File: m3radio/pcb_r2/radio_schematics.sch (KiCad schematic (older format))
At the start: 18 parts, among them IC201 Si4460, P201 COAX

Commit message: update m3radio to si4461 (higher power variant)
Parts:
- IC201: value Si4460 -> Si4461; Farnell 2462635 -> 2462636
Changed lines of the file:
@@
 P 2550 2900
 F 0 "IC201" H 2250 3600 50  0000 L CNN
-F 1 "Si4460" H 2250 2200 50  0000 L CNN
+F 1 "Si4461" H 2250 2200 50  0000 L CNN
 F 2 "agg:QFN-20-EP-SI" H 2250 2100 50  0001 L CNN
 F 3 "" H 2150 3500 50  0001 C CNN
-F 4 "2462635" H 2250 2000 50  0001 L CNN "Farnell"
+F 4 "2462636" H 2250 2000 50  0001 L CNN "Farnell"
 	1    2550 2900
 	1    0    0    -1

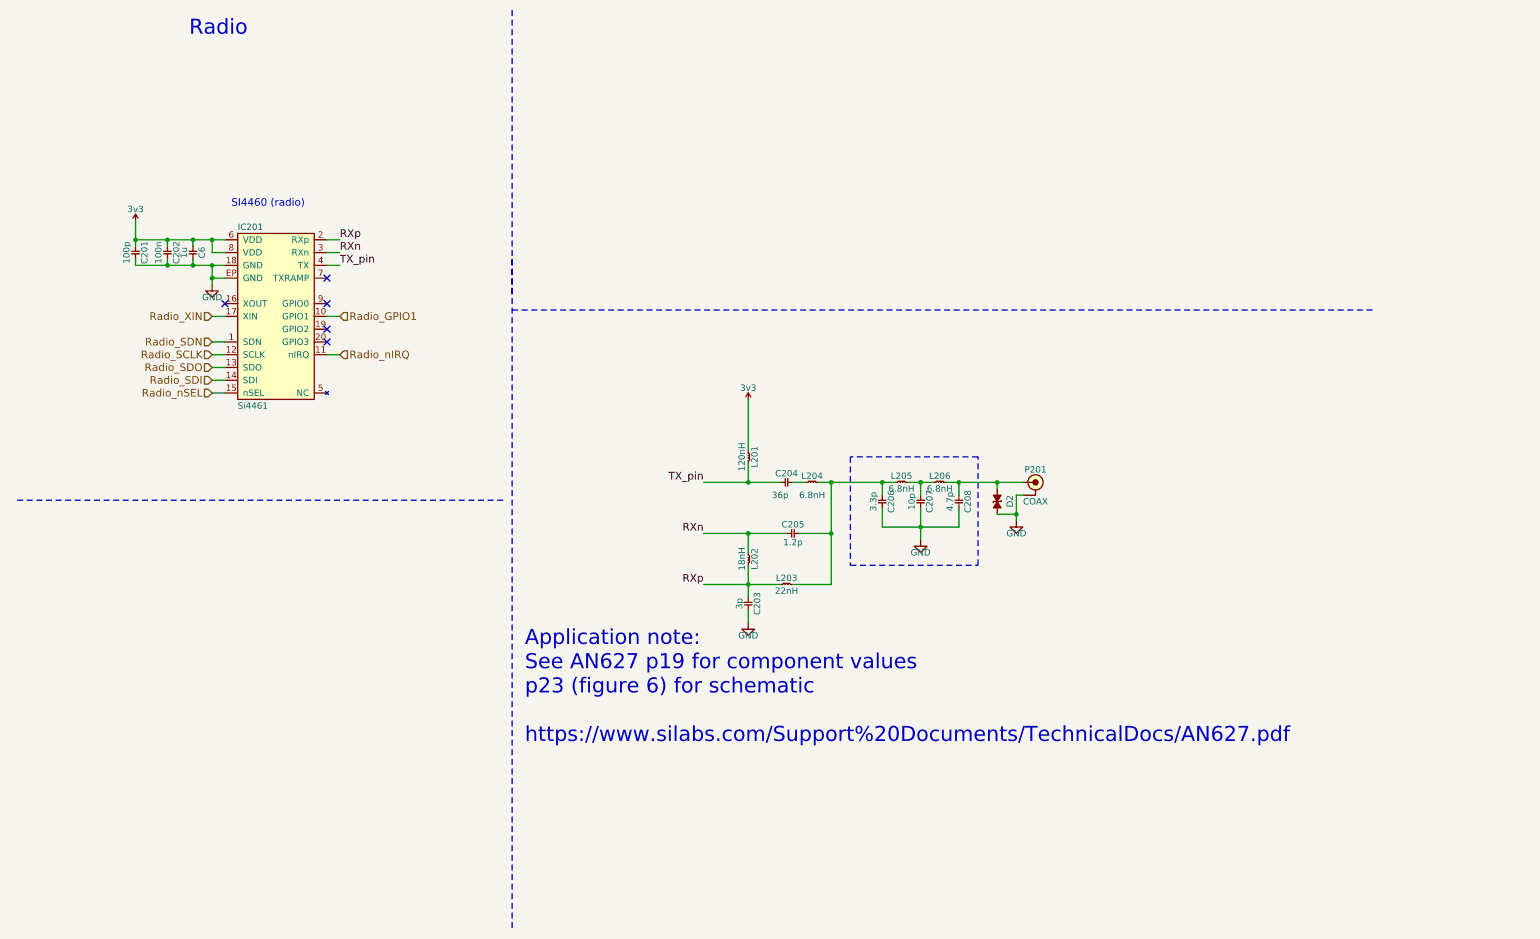
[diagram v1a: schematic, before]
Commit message: Add potential divider and small changes to radio pcb
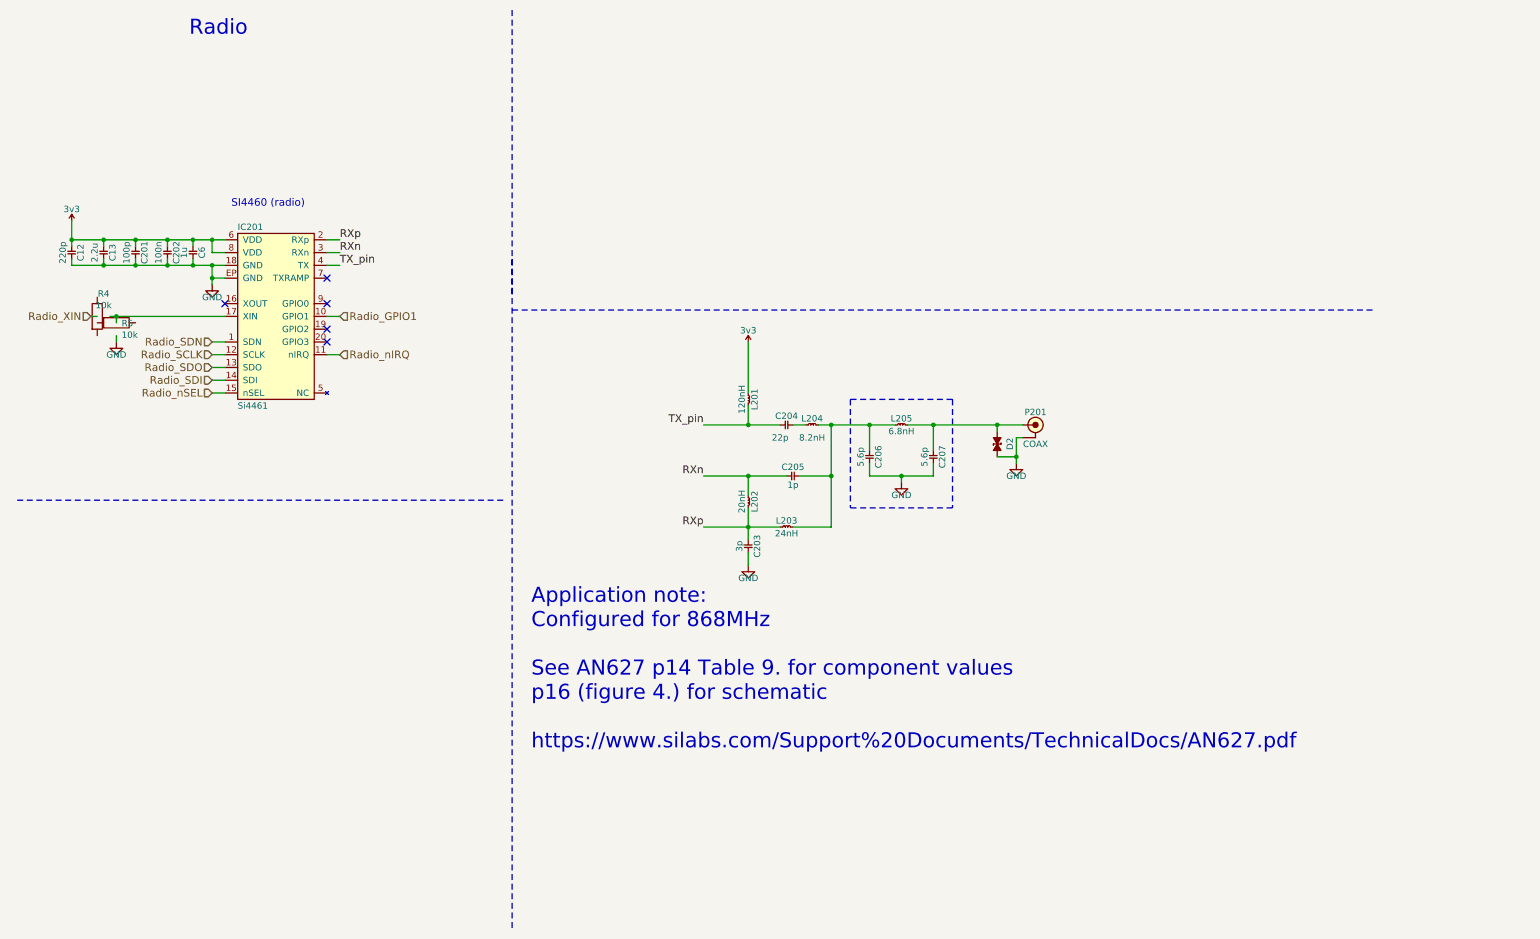
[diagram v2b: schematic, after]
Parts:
- removed C208: 4.7p, agg:0402, symbol C
- removed L206: 6.8nH, agg:0603-L, symbol L
- added C12: 220p, agg:0402, symbol C
- added C13: 2.2u, agg:0402, symbol C
- added R4, R5: 10k, agg:0402, symbol R
- C203: Farnell 2210752 -> 2524984
- C204: value 36p -> 22p; Farnell 1865427 -> 1885344
- C205: value 1.2p -> 1p; Farnell 2218843 -> 2133992
- C206: value 3.3p -> 5.6p; Farnell 2434610 -> 2310316
- C207: value 10p -> 5.6p; Farnell 2496790 -> 2310316
- L202: value 18nH -> 20nH; footprint agg:0603-L -> agg:0402; Farnell 2424720 -> 1748728
- L203: value 22nH -> 24nH; footprint agg:0603-L -> agg:0402; Farnell 1711755 -> 2470344
- L204: value 6.8nH -> 8.2nH; Farnell 1515395 -> 6581778
- L205: footprint agg:0603-L -> agg:0402; Farnell 1515395 -> 1762612
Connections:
- wire segments 49 -> 54
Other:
- note added: "Application note:\nConfigured for 868MHz\n\nSee AN627 p14 Table 9. for component values\np16 (figure 4.) for schematic\n\nhttps://www.silabs.com/Support%20Documents/TechnicalDocs/AN627.pdf"
- note removed: "Application note:\nSee AN627 p19 for component values\np23 (figure 6) for schematic\n\nhttps://www.silabs.com/Support%20Documents/TechnicalDocs/AN627.pdf"
- moved on the sheet: C203, C204, C205, C206, C207, D2, L201, L202, L203, L204, L205, P201
